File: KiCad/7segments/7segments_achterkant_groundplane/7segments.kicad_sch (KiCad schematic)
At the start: 25 parts, among them J1 Conn_01x04_Female, J2 12V DC, J3 R pinnen RGB strips, SW1 ENABLE, SW2 BOOT, T1 BC848, T2 BC848, T3 BC848, T4 BC848, T5 BC848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

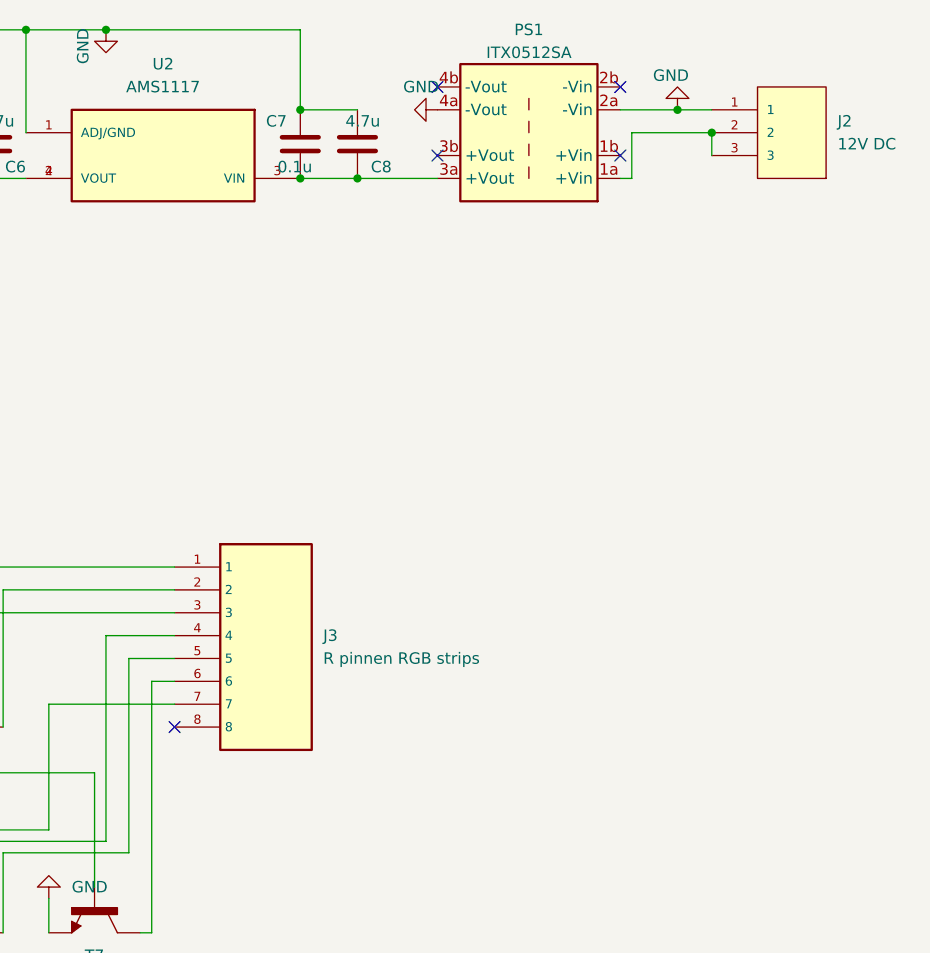
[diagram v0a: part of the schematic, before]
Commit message: aanpassingen aan kicad ontwerpen van 7segment en buffer
toevoeging van groundplanes
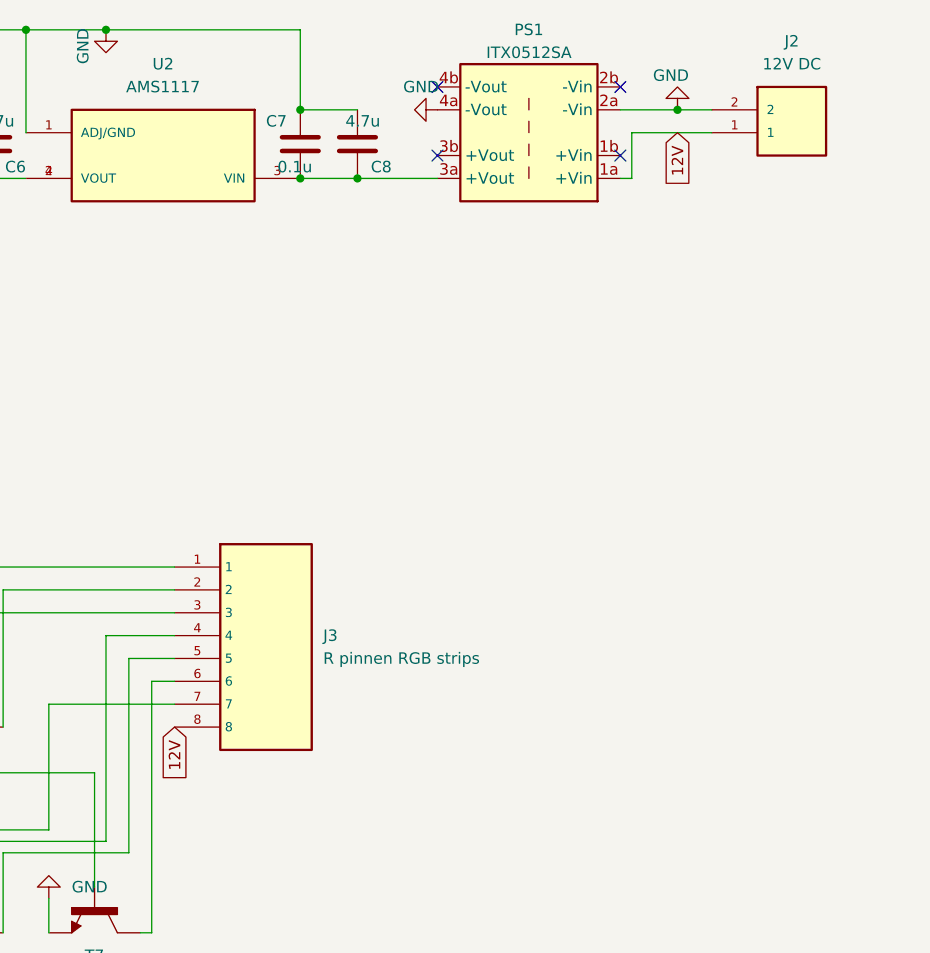
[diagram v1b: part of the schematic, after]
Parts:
- removed J2: 12V DC, libraries:TE_282841-3, symbol 282841-3:282841-3
- added J2: 12V DC, libraries:TE_282841-2, symbol 282841-2:282841-2
- C1: footprint Capacitor_SMD:C_0805_2012Metric -> (none)
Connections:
- net GND: now also J2.2
- net 12V: now reaches J3.8
- net 12V: now also PS1.1a (+Vin), J2.1
- no-connect marks 21 -> 20
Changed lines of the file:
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@@
   (junction (at 53.34 83.82) (diameter 0) (color 0 0 0 0)
-  )
-  (junction (at 226.06 50.8) (diameter 0) (color 0 0 0 0)
   )
   (junction (at 158.75 39.37) (diameter 0) (color 0 0 0 0)
@@
   (no_connect (at 195.58 45.72))
   (no_connect (at 215.9 53.34))
-  (no_connect (at 166.37 116.84))
   (no_connect (at 60.96 101.6))
   (no_connect (at 60.96 104.14))
@@
     (stroke (width 0) (type default) (color 0 0 0 0))
   )
-  (wire (pts (xy 226.06 50.8) (xy 226.06 53.34))
-    (stroke (width 0) (type default) (color 0 0 0 0))
-  )
   (wire (pts (xy 146.05 39.37) (xy 146.05 48.26))
     (stroke (width 0) (type default) (color 0 0 0 0))
@@
   (wire (pts (xy 55.88 83.82) (xy 60.96 83.82))
     (stroke (width 0) (type default) (color 0 0 0 0))
+  )
+  (global_label "12V" (shape input) (at 222.25 50.8 270) (fields_autoplaced)
+    (effects (font (size 1.27 1.27)) (justify right))
+    (property "Intersheet References" "${INTERSHEET_REFS}" (id 0) (at 222.1706 56.7207 90)
+      (effects (font (size 1.27 1.27)) (justify right) hide)
+    )
+  )
+  (global_label "12V" (shape input) (at 166.37 116.84 270) (fields_autoplaced)
+    (effects (font (size 1.27 1.27)) (justify right))
+    (property "Intersheet References" "${INTERSHEET_REFS}" (id 0) (at 166.2906 122.7607 90)
+      (effects (font (size 1.27 1.27)) (justify right) hide)
+    )
   )
   (symbol (lib_id "power:GND") (at 127 48.26 180) (unit 1)
@@
   (symbol (lib_id "power:GND") (at 222.25 48.26 180) (unit 1)
     (in_bom yes) (on_board yes)
-    (property "Reference" "#PWR?" (id 0) (at 222.25 41.91 0)
+    (property "Reference" "#PWR0110" (id 0) (at 222.25 41.91 0)
       (effects (font (size 1.27 1.27)) hide)
     )
@@
     (pin "1")
   )
+  (symbol (lib_id "282841-2:282841-2") (at 236.22 48.26 0) (mirror x) (unit 1)
+    (in_bom yes) (on_board yes) (fields_autoplaced)
+    (property "Reference" "J2" (id 0) (at 234.95 40.64 0))
+    (property "Value" "12V DC" (id 1) (at 234.95 43.18 0))
+    (property "Footprint" "libraries:TE_282841-2" (id 2) (at 236.22 48.26 0)
+      (effects (font (size 1.27 1.27)) (justify left bottom) hide)
+    )
+    (property "Datasheet" "" (id 3) (at 236.22 48.26 0)
+      (effects (font (size 1.27 1.27)) (justify left bottom) hide)
+    )
+    (property "Comment" "282841-2" (id 4) (at 236.22 48.26 0)
+      (effects (font (size 1.27 1.27)) (justify left bottom) hide)
+    )
+    (property "EU_RoHS_Compliance" "Compliant with Exemptions" (id 5) (at 236.22 48.26 0)
+      (effects (font (size 1.27 1.27)) (justify left bottom) hide)
+    )
+    (pin "1")
+    (pin "2")
+  )
   (symbol (lib_id "power:GND") (at 55.88 116.84 0) (unit 1)
     (in_bom yes) (on_board yes)
@@
     (pin "3")
   )
-  (symbol (lib_id "282841-3:282841-3") (at 236.22 50.8 0) (mirror y) (unit 1)
-    (in_bom yes) (on_board yes) (fields_autoplaced)
-    (property "Reference" "J2" (id 0) (at 240.03 49.5299 0)
-      (effects (font (size 1.27 1.27)) (justify right))
-    )
-    (property "Value" "12V DC" (id 1) (at 240.03 52.0699 0)
-      (effects (font (size 1.27 1.27)) (justify right))
-    )
-    (property "Footprint" "libraries:TE_282841-3" (id 2) (at 236.22 50.8 0)
-      (effects (font (size 1.27 1.27)) (justify left bottom) hide)
-    )
-    (property "Datasheet" "" (id 3) (at 236.22 50.8 0)
-      (effects (font (size 1.27 1.27)) (justify left bottom) hide)
-    )
-    (property "Comment" "282841-3" (id 4) (at 236.22 50.8 0)
-      (effects (font (size 1.27 1.27)) (justify left bottom) hide)
-    )
-    (property "EU_RoHS_Compliance" "Compliant with Exemptions" (id 5) (at 236.22 50.8 0)
-      (effects (font (size 1.27 1.27)) (justify left bottom) hide)
-    )
-    (pin "1")
-    (pin "2")
-    (pin "3")
-  )
   (symbol (lib_id "AMS1117:AMS1117") (at 165.1 53.34 180) (unit 1)
     (in_bom yes) (on_board yes) (fields_autoplaced)
@@
       (effects (font (size 1.27 1.27)) (justify right))
     )
-    (property "Footprint" "Capacitor_SMD:C_0805_2012Metric" (id 2) (at 105.7148 48.26 0)
+    (property "Footprint" "" (id 2) (at 105.7148 48.26 0)
       (effects (font (size 1.27 1.27)) hide)
     )
@@
     )
     (path "/1c21c6f5-3e71-4be3-bf45-d619c41235dc"
-      (reference "#PWR?") (unit 1) (value "GND") (footprint "")
+      (reference "#PWR0110") (unit 1) (value "GND") (footprint "")
     )
     (path "/ca3bfd12-a47a-49d0-a984-db6af30b3c2f"
-      (reference "C1") (unit 1) (value "220u") (footprint "Capacitor_SMD:C_0805_2012Metric")
+      (reference "C1") (unit 1) (value "220u") (footprint "libraries:CAP_EEE0JA101WR")
     )
     (path "/4f6e295a-eda9-488f-8a54-b432f357af54"
@@
       (reference "J1") (unit 1) (value "Conn_01x04_Female") (footprint "Connector_PinHeader_2.54mm:PinHeader_1x04_P2.54mm_Vertical")
     )
-    (path "/9d86002a-4404-4832-bfc8-aaaacfcac63c"
-      (reference "J2") (unit 1) (value "12V DC") (footprint "libraries:TE_282841-3")
+    (path "/53ded23b-dad2-4c6d-9d77-91fa13f8ed66"
+      (reference "J2") (unit 1) (value "12V DC") (footprint "libraries:TE_282841-2")
     )
     (path "/1842b158-5de9-40ef-b815-cc6428c97c75"
